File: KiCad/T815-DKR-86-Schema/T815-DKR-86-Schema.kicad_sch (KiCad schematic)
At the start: 46 parts, among them M1 RC Model Motor, Q10 BS170, Q11 BS170, Q3 BS170, Q7 BS170, Q8 BS170, Q9 BS170, U1 Optocoupler_Module, U2 Optocoupler_Module, U3 PWM_MOSFET_Module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

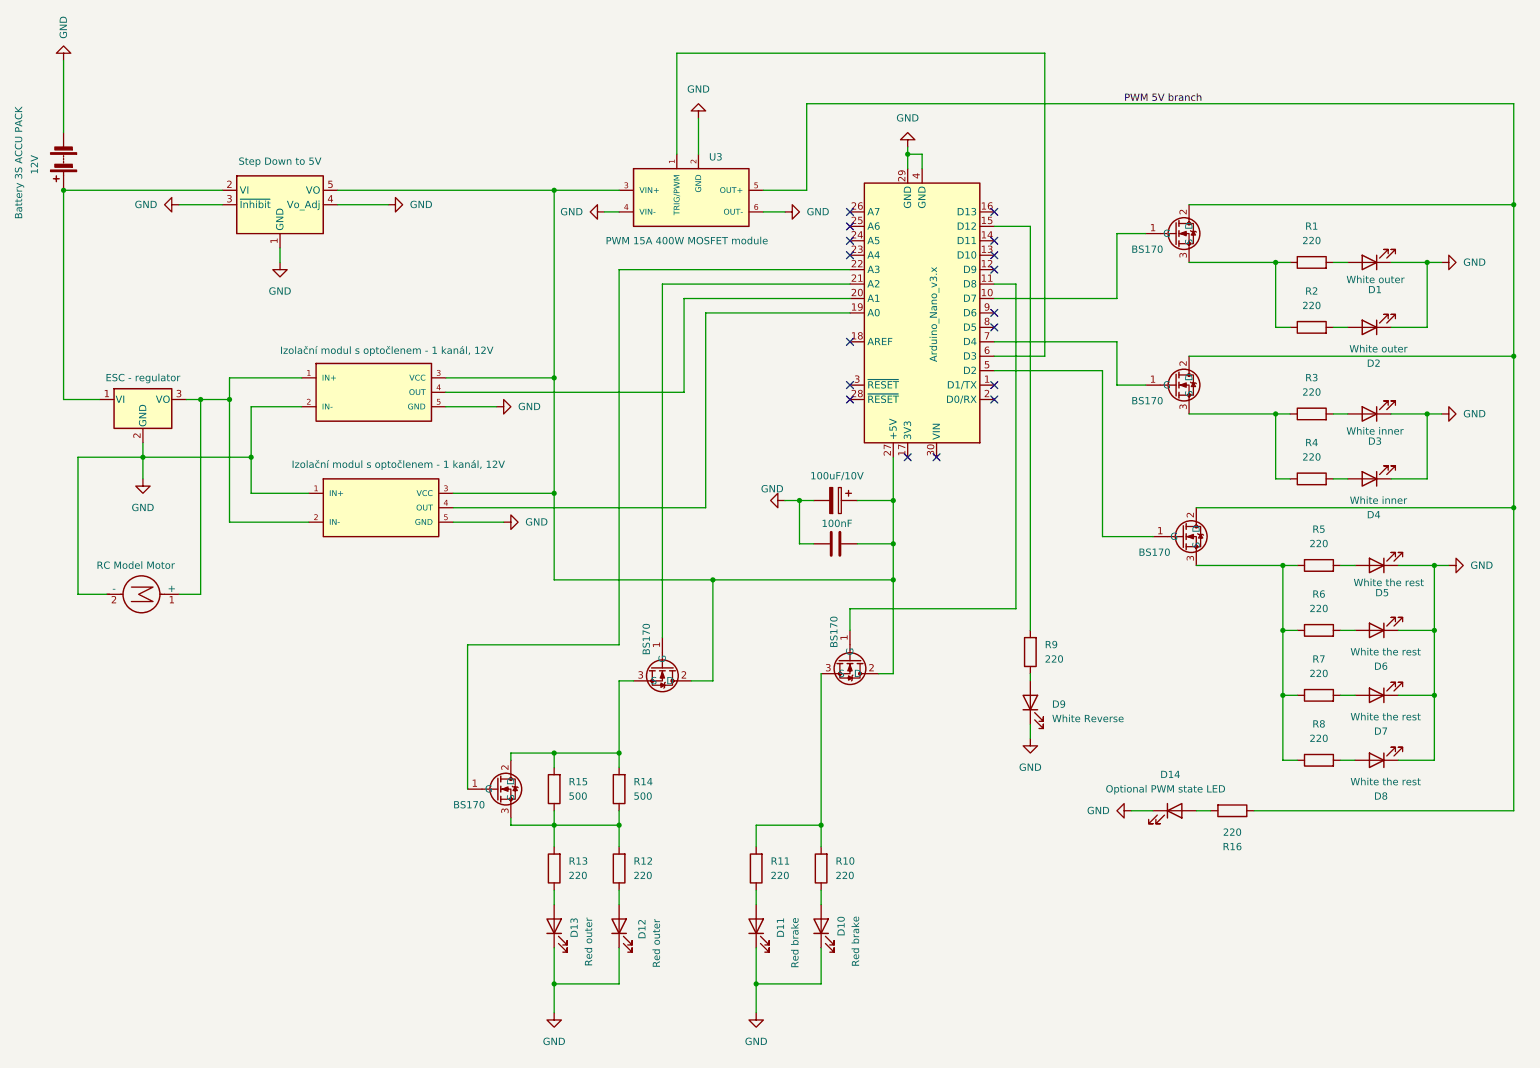
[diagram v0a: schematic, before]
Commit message: Removing dependency on information that motor is spinning forward. Thes light module does not need that information.
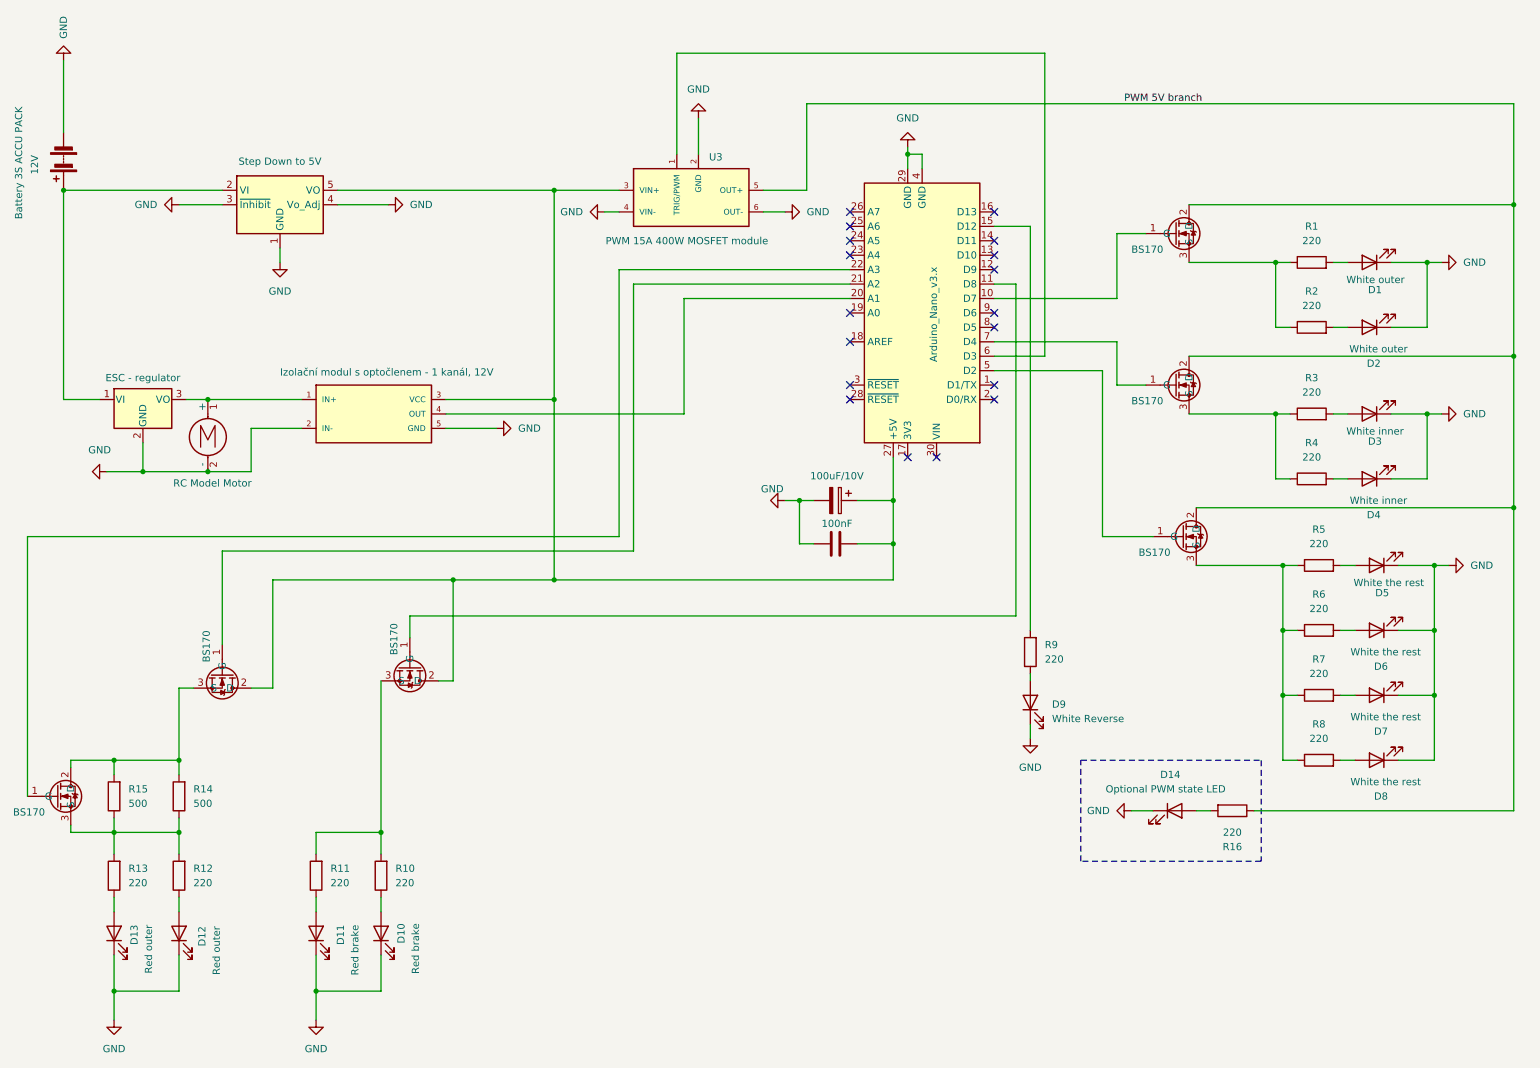
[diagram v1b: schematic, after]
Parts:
- removed U2: Optocoupler_Module, symbol T815-DKR-86:Optocoupler_Module
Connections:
- no-connect marks 17 -> 18
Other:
- moved on the sheet: D10, D11, D12, D13, R10, R11, R12, R13, R14, R15

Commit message: revised version. corrected transistors connections.
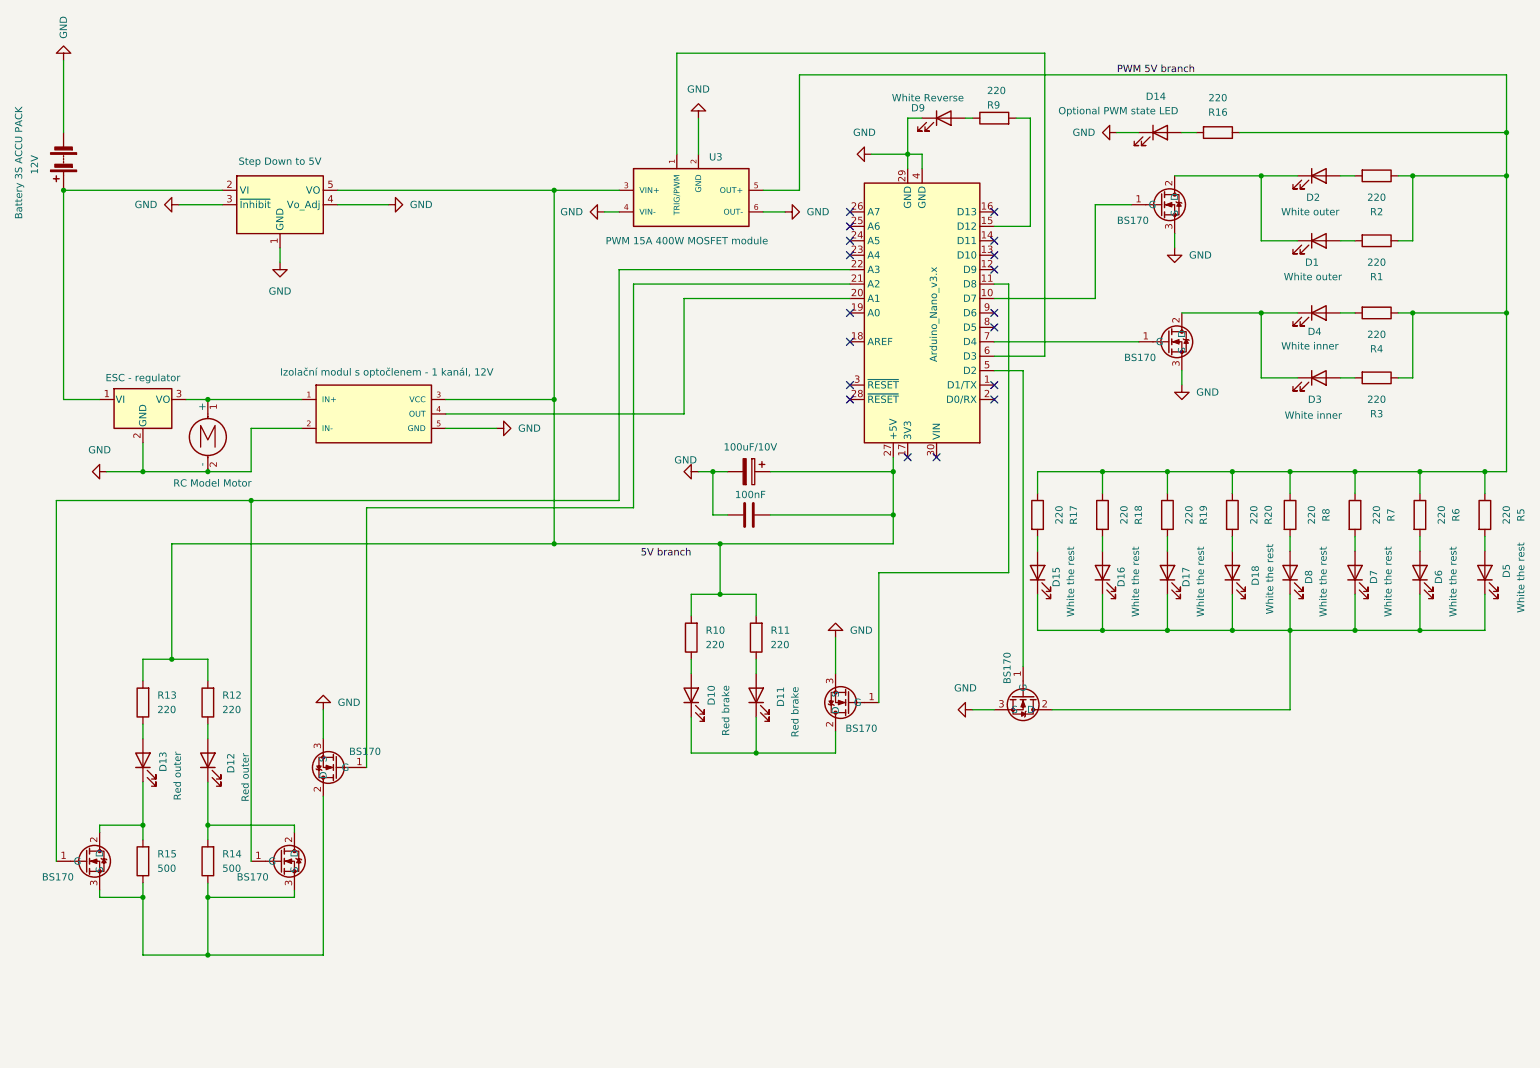
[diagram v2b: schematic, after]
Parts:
- removed Q3: BS170, Package_TO_SOT_THT:TO-220-3_Vertical, symbol Transistor_FET:IRLZ44N
- added D15, D16, D17, D18: White the rest, symbol Device:LED
- added Q1, Q2: BS170, Package_TO_SOT_THT:TO-220-3_Vertical, symbol Transistor_FET:IRLZ44N
- added R17, R18, R19, R20: 220, symbol Device:R
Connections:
- net GND: now also Q10.3 (S), Q11.3 (S), Q7.3 (S), Q8.3 (S), Q9.3 (S); no longer D1.1 (K), D10.1 (K), D11.1 (K), D12.1 (K), D13.1 (K), D2.1 (K), D3.1 (K), D4.1 (K), D5.1 (K), D6.1 (K), D7.1 (K), D8.1 (K)
- net PWM 5V branch: now also R1.1, R2.1, R3.1, R4.1, R5.1, R6.1, R7.1, R8.1, R17.1, R18.1, R19.1, R20.1; no longer Q10.2 (D), Q11.2 (D), Q9.2 (D)
- net at R12.2, R13.2: now also A1.27 (+5V), C1.1, C2.2, R10.2, R11.2, U1.3 (VCC), U3.3 (VIN+), U5.5 (VO); no longer R14.1, R15.1
- net at A1.22 (A3): now also Q1.1 (G), Q2.1 (G)
- new net: D17.2 (A), R19.2
- new net: D15.1 (K), D16.1 (K), D17.1 (K), D18.1 (K), D5.1 (K), D6.1 (K), D7.1 (K), D8.1 (K), Q9.2 (D)
- new net: D3.1 (K), D4.1 (K), Q10.2 (D)
- new net: Q1.3 (S), Q2.3 (S), Q7.2 (D), R14.1, R15.1
- new net: D10.1 (K), D11.1 (K), Q8.2 (D)
- new net: D18.2 (A), R20.2
- new net: D15.2 (A), R17.2
- new net: D1.1 (K), D2.1 (K), Q11.2 (D)
- new net: D16.2 (A), R18.2
- new net: D12.1 (K), Q1.2 (D), R14.2
- new net: D13.1 (K), Q2.2 (D), R15.2
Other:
- moved on the sheet: D1, D10, D11, D12, D13, D14, D2, D3, D4, D5, D6, D7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
